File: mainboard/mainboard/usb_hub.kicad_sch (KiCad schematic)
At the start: 18 parts, among them U7 hs8836a

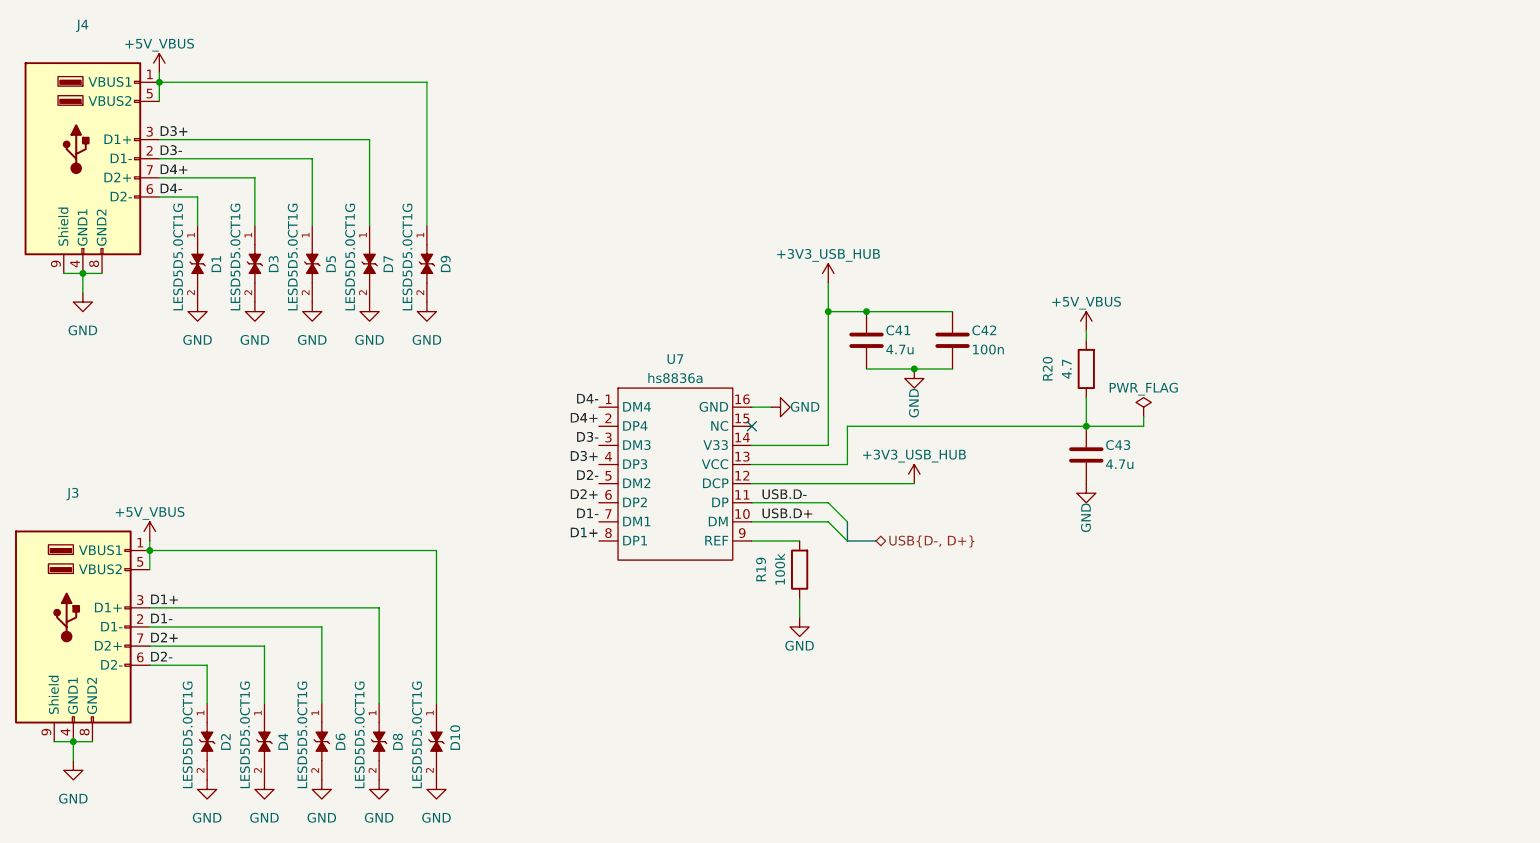
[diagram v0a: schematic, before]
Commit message: Share KiCad libraries, update v2.5 mainboard schematics
- Move every board's symbols, footprints and 3D models into libs/ and point
  the projects' lib tables there; add the mspc design-block library.
- Mainboard: new debug probe, MSPC bus and power connector sheets; drop the
  old shared-bus, south/north bridge and SD card sheets.
- Remove orphaned sheets from the GPU cards and the simulation sandbox.
- Rewrite the v2.5 plan, document libs/ in the README, ignore KiCad 10
  restore backups.

Co-Authored-By: Claude Opus 5 (1M context) <noreply@anthropic.com>
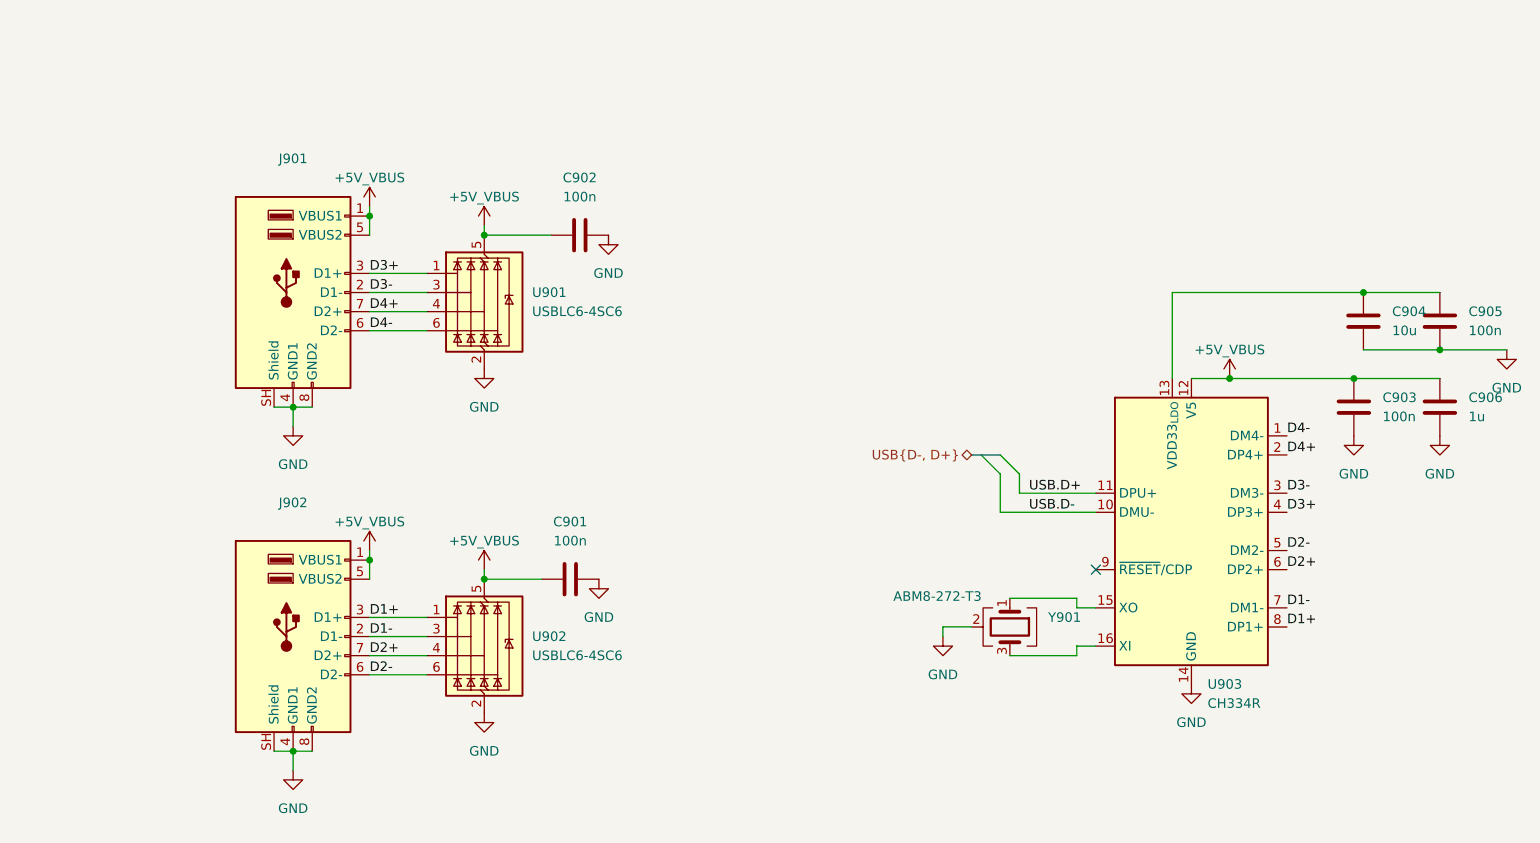
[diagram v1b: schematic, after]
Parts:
- removed C41, C43: 4.7u, Capacitor_SMD:C_0402_1005Metric_Pad0.74x0.62mm_HandSolder, symbol Device:C
- removed C42: 100n, Capacitor_SMD:C_0402_1005Metric_Pad0.74x0.62mm_HandSolder, symbol Device:C
- removed D1, D10, D2, D3, D4, D5, D6, D7, D8, D9: LESD5D5.0CT1G, footprints:TVS_LESD5D5.0CT1G, symbol LESD5D5.0CT1G:LESD5D5.0CT1G
- removed R19: 100k, Resistor_SMD:R_0402_1005Metric_Pad0.72x0.64mm_HandSolder, symbol Device:R
- removed R20: 4.7, Resistor_SMD:R_0402_1005Metric_Pad0.72x0.64mm_HandSolder, symbol Device:R
- removed U7: hs8836a, Package_SO:SOP-16_3.9x9.9mm_P1.27mm, symbol HS8836A:hs8836a
- added C901, C902, C903, C905: 100n, Capacitor_SMD:C_0402_1005Metric_Pad0.74x0.62mm_HandSolder, symbol Device:C
- added C904: 10u, Capacitor_SMD:C_1206_3216Metric_Pad1.33x1.80mm_HandSolder, symbol Device:C
- added C906: 1u, Capacitor_SMD:C_0402_1005Metric_Pad0.74x0.62mm_HandSolder, symbol Device:C
- added U901, U902: USBLC6-4SC6, Package_TO_SOT_SMD:SOT-23-6, symbol Power_Protection:USBLC6-4SC6
- added U903: CH334R, Package_SO:QSOP-16_3.9x4.9mm_P0.635mm, symbol Interface_USB:CH334R
- added Y901: ABM8-272-T3, Crystal:Crystal_SMD_3225-4Pin_3.2x2.5mm, symbol mspc_xtal:ABM8-272-T3
- renumbered J4 to J901, J3 to J902
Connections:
- net +5V_VBUS: now also C901.1, C902.1, C903.2, C906.1, U901.5 (VBUS), U902.5 (VBUS), U903.12 (V5)
- net D1+: now also U902.1 (I/O1), U903.8 (DP1+)
- net D1-: now also U902.3 (I/O2), U903.7 (DM1-)
- net D2+: now also U902.4 (I/O3), U903.6 (DP2+)
- net D2-: now also U902.6 (I/O4), U903.5 (DM2-)
- net D3+: now also U901.1 (I/O1), U903.4 (DP3+)
- net D3-: now also U901.3 (I/O2), U903.3 (DM3-)
- net D4+: now also U901.4 (I/O3), U903.2 (DP4+)
- net D4-: now also U901.6 (I/O4), U903.1 (DM4-)
- net GND: now also J901.SH (Shield), J902.SH (Shield), C901.2, C902.2, C903.1, C904.2, C905.1, C906.2, U901.2 (GND), U902.2 (GND), U903.14 (GND), Y901.2 (G), Y901.4 (G); no longer J901.9 (Shield), J902.9 (Shield)
- net USB.D+: now also U903.11 (DPU+)
- net USB.D-: now also U903.10 (DMU-)
- new net: C904.1, C905.2, U903.13 (VDD33_{LDO})
- new net: U903.15 (XO), Y901.1
- new net: U903.16 (XI), Y901.3
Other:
- moved on the sheet: J901, J902

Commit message: Mainboard v3: schematic review fixes
New sheets for the housekeeping bus: TCA6408A expander, INA226/INA3221
power measurement and the MCP7940N RTC with a CR1220 backup cell.

Correctness:
- RTC load caps C241/C242 are 6.8 pF C0G 0402 (were a relay footprint).
- L50 is the AOTA-B201610S3R3-101-T with pin 1 on +1V1_MCU; U52 is an
  APS1604M-3SQR-SN on a 150-mil SOP-8.
- I2S is DIN=GPIO13, BCK=GPIO14, LRCK=GPIO15, as pico-extras audio_i2s
  expects. Expander INT# goes to GPIO42.
- ADC_AVDD filter (FB50, C74, C75), 33 ohm on SDIO CLK, SD ESD (U53/U54),
  PSRAM 1 uF, POWER_BUTTON 10 k pull-up, 10 uF at the SY6280 inputs.
- J_DBG: USBLC6-4SC6 on the probe USB, 47 uF polymer on +5V_DBG against
  charger overvoltage spikes, and bleeders on both USB-C VBUS inputs and
  on +5V_DBG.
- Power symbols point at their matching project_power symbols.

Parts and fields:
- Part numbers and LCSC codes for the purchased parts: push-push microSD
  J53, HRO USB-C J1/J2, stacked USB-A J90/J91, TLV70033DDCR, and others.
- Voltage, dielectric and tolerance fields on every capacitor and a
  tolerance on every resistor; the field is named "LCSC" everywhere.
- Hand-solder footprint variants where KiCad has one.

Drawing:
- References renumbered into the per-sheet ranges.
- Net names on the USB, crystal, DAC, CC and ISET nets; netclass
  patterns updated.
- No four-way junctions left.
- Notes for the slot pin 1 marking, J120 and firmware bring-up.

ERC is clean with all rules enabled.

Co-Authored-By: Claude Opus 5 (1M context) <noreply@anthropic.com>
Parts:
- C90: renamed from C902; Dielectric (none) -> X7R; Tolerance (none) -> 10%; Voltage (none) -> 16V
- C91: renamed from C901; Dielectric (none) -> X7R; Tolerance (none) -> 10%; Voltage (none) -> 16V
- C92: renamed from C904; Dielectric (none) -> X5R; LCSC (none) -> C9807; MPN (none) -> CL31A106KAHNNNE; Tolerance (none) -> 10%; Voltage (none) -> 25V
- C93: renamed from C903; Dielectric (none) -> X7R; Tolerance (none) -> 10%; Voltage (none) -> 16V
- C94: renamed from C905; Dielectric (none) -> X7R; Tolerance (none) -> 10%; Voltage (none) -> 16V
- C95: renamed from C906; Dielectric (none) -> X5R; Tolerance (none) -> 10%; Voltage (none) -> 16V
- J90: renamed from J901; value (none) -> USB_A_Stacked; LCSC (none) -> C12049; MPN (none) -> 907-111A1022D10200; Manufacturer (none) -> Jing Extension
- J91: renamed from J902; value (none) -> USB_A_Stacked; LCSC (none) -> C12049; MPN (none) -> 907-111A1022D10200; Manufacturer (none) -> Jing Extension
- U90: renamed from U901; footprint Package_TO_SOT_SMD:SOT-23-6 -> Package_TO_SOT_SMD:SOT-23-6_Handsoldering; LCSC (none) -> C111212; MPN (none) -> USBLC6-4SC6; Manufacturer (none) -> STMicroelectronics
- U91: renamed from U902; footprint Package_TO_SOT_SMD:SOT-23-6 -> Package_TO_SOT_SMD:SOT-23-6_Handsoldering; LCSC (none) -> C111212; MPN (none) -> USBLC6-4SC6; Manufacturer (none) -> STMicroelectronics
- U92: renamed from U903; LCSC (none) -> C4154405; MPN (none) -> CH334R; Manufacturer (none) -> WCH
- Y90: renamed from Y901; footprint Crystal:Crystal_SMD_3225-4Pin_3.2x2.5mm -> Crystal:Crystal_SMD_3225-4Pin_3.2x2.5mm_HandSoldering; LCSC (none) -> C20625731
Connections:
- net HUB_VDD33: now reaches C92.1, C94.2, U92.13 (VDD33_{LDO})
- net HUB_XO: now reaches U92.15 (XO), Y90.1
- net HUB_XI: now reaches U92.16 (XI), Y90.3

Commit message: Mainboard: title blocks for v3
Every schematic sheet and the PCB carry the same title block: "MSPC
mainboard", rev 3, 2026-09-13. The root sheet still said rev 1 from
2022, and most sheets had none.

Co-Authored-By: Claude Opus 5 (1M context) <noreply@anthropic.com>
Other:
- company: (none) -> Mateusz Stadnik
- title: (none) -> MSPC mainboard
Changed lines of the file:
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@@
 	(generator_version "10.0")
 	(paper "A4")
+	(title_block
+		(title "MSPC mainboard")
+		(date "2026-09-13")
+		(rev "3")
+		(company "Mateusz Stadnik")
+	)
 	(junction
 		(at 72.39 88.9)
